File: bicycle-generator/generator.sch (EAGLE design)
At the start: 61 parts, among them IC1 MC34063AD, K1 ARK500/2, K2 ARK500/2, K3 ARK500/2, K4 ARK500/2, K5 ARK500/2, K6 HEAT_NPN, K7 ARK500/2, K8 ARK500/2, Q1 IRF3704S, Q4 IRFR5305, T1 BC807, T2 BC807, X1 CV_LED, X2 PWR_LED, X3 5V_SW, X4 5V_LED, X5 5V_OUT

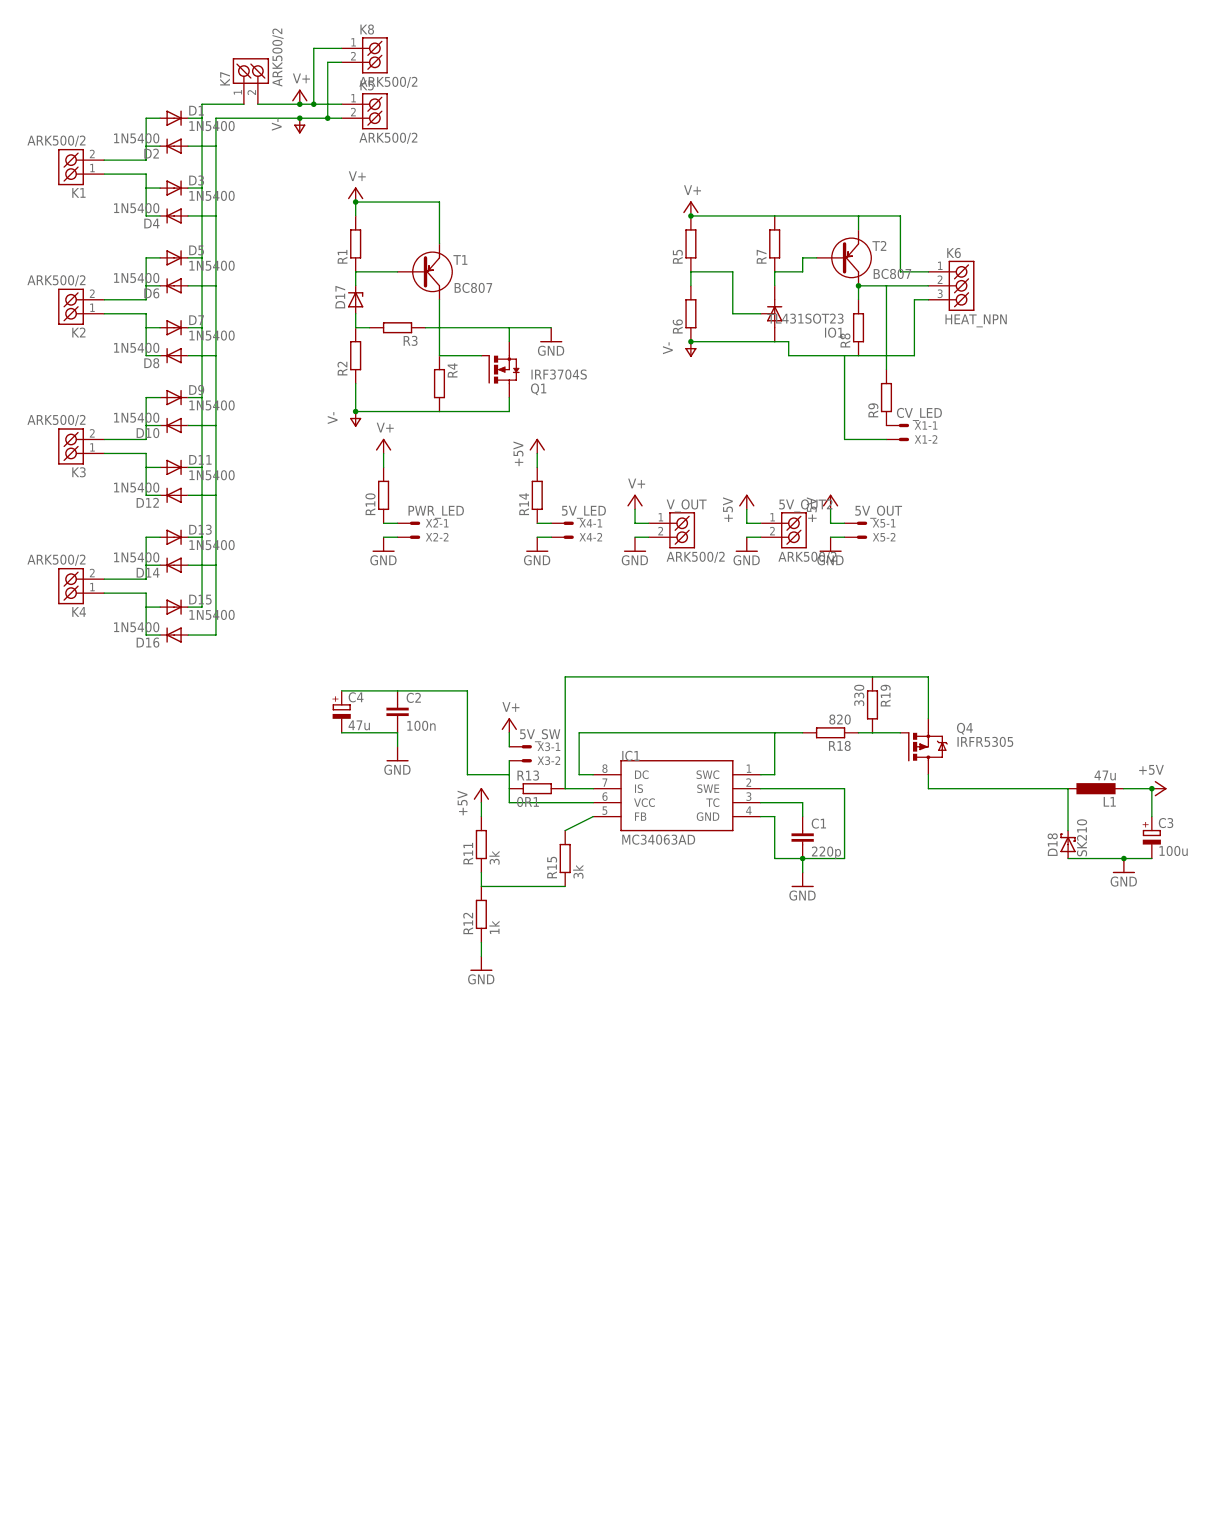
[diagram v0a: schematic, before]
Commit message: Use N-channel MOSFET with pulldown.
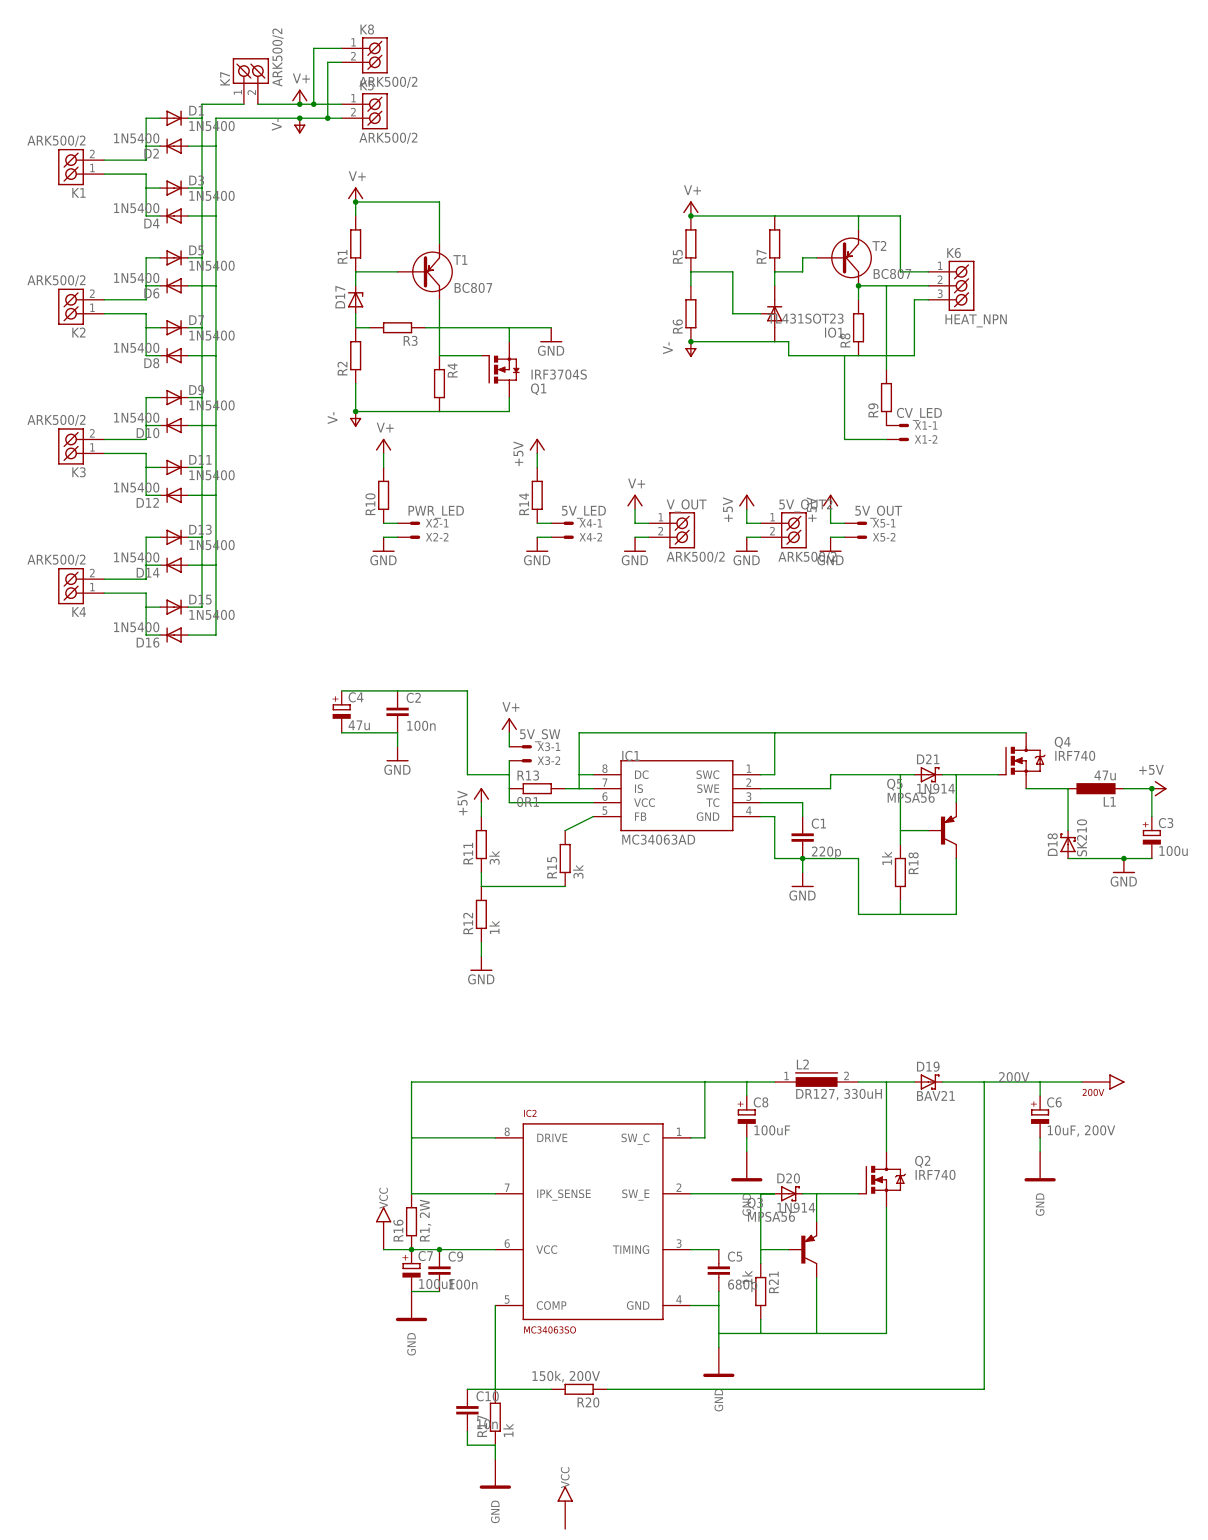
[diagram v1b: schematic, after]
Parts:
- removed R19: 330, rcl:R-EU_R0805
- added C10: 10n, rcl:C-EUC0805
- added C5: 680p, resistor:C-EUC0805
- added C6: 10uF, 200V, resistor:CPOL-EUE3.5-10
- added C7, C8: 100uF, resistor:CPOL-EUD
- added C9: 100n, rcl:C-EUC0805
- added D19: BAV21, diode:SCHOTTKY-DIODEDO35-7
- added D20, D21: 1N914, diode:SCHOTTKY-DIODEDO35-7
- added IC2: MC34063SO, #Krakonos:MC34063SO
- added L2: DR127, 330uH, inductors:DR127
- added Q2: IRF740, transistor-power:IRF740
- added Q3, Q5: MPSA56, transistor-pnp:MPSA56
- added R16: R1, 2W, resistor:R-EU_V234/12
- added R17, R21: 1k, resistor:R-EU_R0805
- added R20: 150k, 200V, resistor:R-EU_R0805
- Q4: value IRFR5305 -> IRF740; device transistor-power:IRFR5305 -> transistor-power:IRF740
- R18: value 820 -> 1k; device rcl:R-EU_R0805 -> resistor:R-EU_R0805
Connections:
- new net 200V: C6.+, D19.C, R20.1
- new net N$25: C10.1, IC2.COMP, R17.2, R20.2
- new net N$26: C5.1, IC2.TIMING
- new net N$29: D19.A, L2.2, Q2.D
- new net N$30: D20.C, Q2.G, Q3.E
- new net N$31: D20.A, IC2.SW_E, Q3.B, R21.1
- new net N$32: C8.+, IC2.DRIVE, IC2.IPK_SENSE, IC2.SW_C, L2.1, R16.2
- new net N$33: D21.A, IC1.SWE
- new net VCC: C7.+, C9.1, IC2.VCC, R16.1
- net GND: now also C10.2, C5.2, C6.-, C7.-, C8.-, C9.2, IC2.GND, Q2.S, Q3.C, Q5.C, R17.1, R18.2, R21.2; no longer IC1.SWE
- net N$15: now also D21.C, Q4.G, Q5.E; no longer IC1.DC, IC1.SWC, R18.2
- net N$19: now also Q4.S; no longer Q4.D
- net N$27: now also IC1.DC, IC1.IS, IC1.SWC, Q4.D, R13.2; no longer Q4.G, R18.1, R19.2
- net N$28: now also Q5.B, R18.1; no longer IC1.IS, Q4.S, R13.2, R19.1
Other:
- moved on the sheet: R18

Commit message: First version routed.
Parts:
- removed C10: 10n, rcl:C-EUC0805
- removed C5: 680p, resistor:C-EUC0805
- removed C6: 10uF, 200V, resistor:CPOL-EUE3.5-10
- removed C7, C8: 100uF, resistor:CPOL-EUD
- removed C9: 100n, rcl:C-EUC0805
- removed D20, D21: 1N914, diode:SCHOTTKY-DIODEDO35-7
- removed IC2: MC34063SO, #Krakonos:MC34063SO
- removed L2: DR127, 330uH, inductors:DR127
- removed Q3, Q5: MPSA56, transistor-pnp:MPSA56
- removed Q4: IRF740, transistor-power:IRF740
- removed R16: R1, 2W, resistor:R-EU_V234/12
- removed R17, R21: 1k, resistor:R-EU_R0805
- removed R20: 150k, 200V, resistor:R-EU_R0805
- added T3: (no value), transistor:BC807-16-PNP-SOT23-BEC
- D19: value BAV21 -> LL4148-MINIMELF; device diode:SCHOTTKY-DIODEDO35-7 -> diode:PMLL41SOD80C
- Q2: value IRF740 -> IRF3704S; device transistor-power:IRF740 -> transistor-power:IRF3704S
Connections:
- removed net 200V: C6.+, D19.C, R20.1
- removed net N$25: C10.1, IC2.COMP, R17.2, R20.2
- removed net N$26: C5.1, IC2.TIMING
- removed net N$29: D19.A, L2.2, Q2.D
- removed net N$30: D20.C, Q2.G, Q3.E
- removed net N$31: D20.A, IC2.SW_E, Q3.B, R21.1
- removed net N$32: C8.+, IC2.DRIVE, IC2.IPK_SENSE, IC2.SW_C, L2.1, R16.2
- removed net N$33: D21.A, IC1.SWE
- removed net VCC: C7.+, C9.1, IC2.VCC, R16.1
- net GND: now also T3.C; no longer C10.2, C5.2, C6.-, C7.-, C8.-, C9.2, IC2.GND, Q2.S, Q3.C, Q5.C, R17.1, R21.2
- net N$15: now also D19.C, Q2.G, T3.E; no longer D21.C, Q4.G, Q5.E
- net N$19: now also Q2.S; no longer Q4.S
- net N$27: now also Q2.D; no longer Q4.D
- net N$28: now also D19.A, IC1.SWE, T3.B; no longer Q5.B

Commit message: Routed board.
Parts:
- L1: device rcl:L-EUPIS2816 -> rcl:L-EUTJ3-U1
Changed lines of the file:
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@@
 <part name="C3" library="rcl" deviceset="CPOL-EU" device="D" value="100u"/>
 <part name="C4" library="rcl" deviceset="CPOL-EU" device="D" value="47u"/>
-<part name="L1" library="rcl" deviceset="L-EU" device="PIS2816" value="47u "/>
+<part name="L1" library="rcl" deviceset="L-EU" device="TJ3-U1" value="47u "/>
 <part name="D18" library="diode" deviceset="SCHOTTKY-DIODE" device="SMD" value="SK210"/>
 <part name="SUPPLY5" library="supply2" deviceset="V+" device=""/>
